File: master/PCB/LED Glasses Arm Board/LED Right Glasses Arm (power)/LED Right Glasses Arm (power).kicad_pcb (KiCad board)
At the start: 2 copper layers, 130.8 x 20.4 mm, 27 parts, among them J1 Conn_01x02_Male, J2 Conn_01x01_Male, J3 Conn_01x01_Male, Q1 TP0610T, SW1 SW_SPST, U1 TPS63061DSCT

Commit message: updated board
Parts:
- removed R5: 1M, Resistor_SMD:R_0603_1608Metric
- moved C6 7.16 mm to (178.7, 94.2), turned to 90 degrees
- moved C3 5.70 mm to (185.0, 98.4)
- moved TP_gnd1 2.44 mm to (182.5, 93.6)
- moved R3 0.92 mm to (184.2, 94.1), turned to 270 degrees
- moved R4 0.75 mm to (181.3, 97.5)
- moved R2 0.34 mm to (168.0, 98.8)
- moved D2 0.34 mm to (167.3, 95.2)
- moved C5 0.34 mm to (170.6, 95.5)
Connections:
- R2 pad 2: /PG -> GND
- TP_gnd1 pad 1: /PG -> GND
- U1 pad 5: /PG -> Net-(U1-Pad5)
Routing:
- net /VOUT_5V: track 0.00 -> 39.7 mm
- net GND: track 12.3 -> 0.09 mm, vias 8 -> 6
- net Net-(C3-Pad1): track 4.58 -> 0.00 mm
- net Net-(C5-Pad1): track 2.25 -> 0.00 mm
- net Net-(L1-Pad2): track 5.84 -> 4.32 mm
- net Net-(L1-Pad1): track 5.84 -> 4.35 mm
- net (no net): vias 0 -> 2
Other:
- net class Default: trace_width 0.25 -> 0.8; via_drill 0.4 -> 0.3

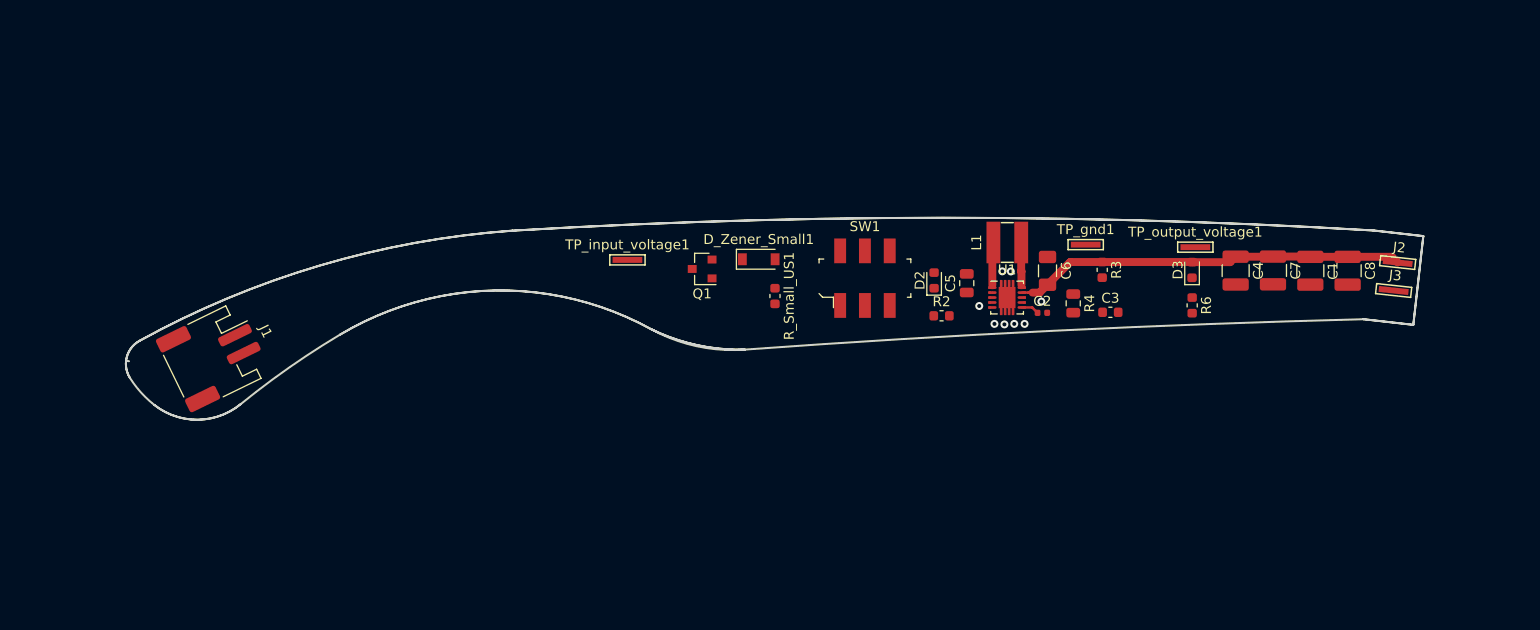
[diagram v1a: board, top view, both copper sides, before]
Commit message: Changes
Test points, routing, need to get the ground plane on the back copper
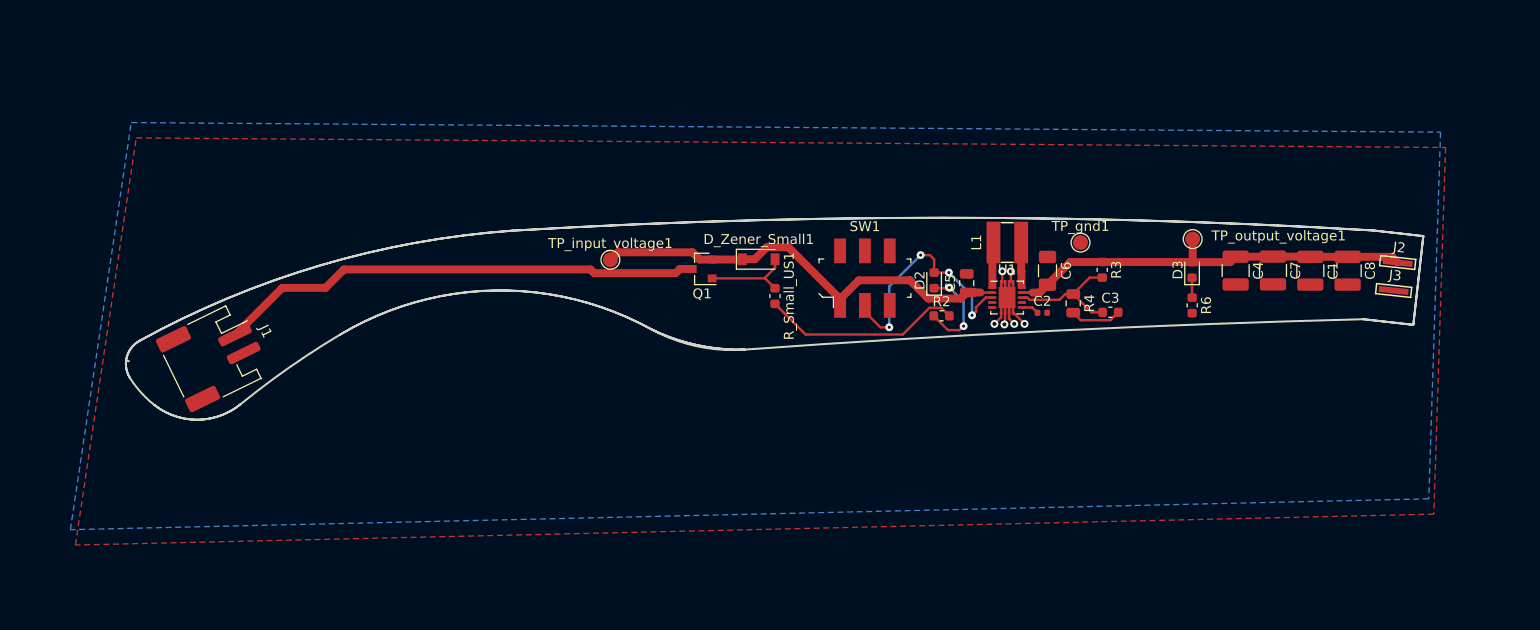
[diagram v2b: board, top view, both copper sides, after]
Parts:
- TP_gnd1, TP_input_voltage1, TP_output_voltage1: footprint Connector_PinHeader_1.00mm:PinHeader_1x01_P1.00mm_Vertical_SMD_CUSTOM -> TestPoint:TestPoint_Pad_D1.5mm
- moved TP_output_voltage1 2.86 mm to (193.3, 91.0)
- moved TP_input_voltage1 2.67 mm to (134.6, 93.1)
- moved TP_gnd1 2.30 mm to (182.0, 91.4)
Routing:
- net /VIN_2.5-12V: track 0.00 -> 49.2 mm
- net Net-(C5-Pad1): track 0.00 -> 44.2 mm
- net GND: track 0.09 -> 34.0 mm
- net Net-(D2-Pad2): track 0.00 -> 25.0 mm, vias 0 -> 4
- net Net-(C3-Pad1): track 0.00 -> 12.9 mm
- net Net-(D2-Pad1): track 0.00 -> 9.82 mm, vias 0 -> 2
- net Net-(D_Zener_Small1-Pad2): track 0.00 -> 9.10 mm
- net /VOUT_5V: track 39.7 -> 42.0 mm
- net Net-(D3-Pad1): track 0.00 -> 2.00 mm
- net (no net): vias 2 -> 0
- added copper zone on B.Cu, net GND
- added copper zone on F.Cu, net GND
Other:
- net class Default: trace_width 0.8 -> 0.25

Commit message: PCB Ready?
Thoughts and Prayers
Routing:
- net GND: track 34.0 -> 44.7 mm, vias 6 -> 10
- net Net-(D2-Pad2): track 25.0 -> 22.8 mm
- net Net-(D2-Pad1): track 9.82 -> 9.22 mm
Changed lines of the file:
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@@
     (thickness 1.6)
     (drawings 25)
-    (tracks 132)
+    (tracks 158)
     (zones 0)
     (modules 26)
@@
   (segment (start 154.318701 100.635901) (end 164.108805 100.635901) (width 0.25) (layer F.Cu) (net 2))
   (segment (start 151.2316 97.5488) (end 154.318701 100.635901) (width 0.25) (layer F.Cu) (net 2))
+  (via (at 178.689 91.186) (size 0.8) (drill 0.3) (layers F.Cu B.Cu) (net 2))
+  (segment (start 178.7017 91.1987) (end 178.689 91.186) (width 0.25) (layer F.Cu) (net 2))
+  (segment (start 174.025 97.7387) (end 174.025 98.3387) (width 0.25) (layer F.Cu) (net 2))
+  (segment (start 174.025 97.6137) (end 174.025 97.7387) (width 0.25) (layer F.Cu) (net 2))
+  (segment (start 173.825 97.4137) (end 174.025 97.6137) (width 0.25) (layer F.Cu) (net 2))
+  (segment (start 173.15 97.4137) (end 173.825 97.4137) (width 0.25) (layer F.Cu) (net 2))
+  (segment (start 175.225 97.7387) (end 175.225 98.3387) (width 0.25) (layer F.Cu) (net 2))
+  (segment (start 175.225 97.6137) (end 175.225 97.7387) (width 0.25) (layer F.Cu) (net 2))
+  (segment (start 175.425 97.4137) (end 175.225 97.6137) (width 0.25) (layer F.Cu) (net 2))
+  (segment (start 176.1 97.4137) (end 175.425 97.4137) (width 0.25) (layer F.Cu) (net 2))
+  (segment (start 174.2598 95.4887) (end 174.1424 95.3713) (width 0.25) (layer F.Cu) (net 2))
+  (segment (start 174.425 95.4887) (end 174.2598 95.4887) (width 0.25) (layer F.Cu) (net 2))
+  (segment (start 174.825 95.4507) (end 175.006 95.2697) (width 0.25) (layer F.Cu) (net 2))
+  (segment (start 174.825 95.4887) (end 174.825 95.4507) (width 0.25) (layer F.Cu) (net 2))
+  (segment (start 173.15 97.4137) (end 172.865 97.4137) (width 0.25) (layer F.Cu) (net 2))
+  (segment (start 172.61141 97.4137) (end 173.15 97.4137) (width 0.25) (layer F.Cu) (net 2))
+  (segment (start 172.39999 97.62512) (end 172.61141 97.4137) (width 0.25) (layer F.Cu) (net 2))
+  (segment (start 172.39999 97.874912) (end 172.39999 97.62512) (width 0.25) (layer F.Cu) (net 2))
+  (segment (start 171.519702 98.7552) (end 172.39999 97.874912) (width 0.25) (layer F.Cu) (net 2))
+  (segment (start 168.8085 98.7552) (end 171.519702 98.7552) (width 0.25) (layer F.Cu) (net 2))
+  (via (at 101.7524 100.7491) (size 0.8) (drill 0.3) (layers F.Cu B.Cu) (net 2))
+  (via (at 170.561 93.1672) (size 0.8) (drill 0.3) (layers F.Cu B.Cu) (net 2))
+  (segment (start 170.561 94.5284) (end 170.561 93.1672) (width 0.25) (layer F.Cu) (net 2))
+  (via (at 184.3151 91.3765) (size 0.8) (drill 0.3) (layers F.Cu B.Cu) (net 2))
   (via (at 168.8084 95.9104) (size 0.8) (drill 0.3) (layers F.Cu B.Cu) (net 3))
   (segment (start 167.2717 95.974) (end 168.7448 95.974) (width 0.25) (layer F.Cu) (net 3))
   (segment (start 168.7448 95.974) (end 168.8084 95.9104) (width 0.25) (layer F.Cu) (net 3))
-  (via (at 170.2435 99.7966) (size 0.8) (drill 0.3) (layers F.Cu B.Cu) (net 3))
   (segment (start 168.8084 95.9104) (end 170.2435 97.3455) (width 0.25) (layer B.Cu) (net 3))
-  (segment (start 170.2435 97.3455) (end 170.2435 99.7966) (width 0.25) (layer B.Cu) (net 3))
+  (via (at 169.9895 99.4802) (size 0.8) (drill 0.3) (layers F.Cu B.Cu) (net 3))
+  (segment (start 170.2435 97.3455) (end 170.2435 99.2262) (width 0.25) (layer B.Cu) (net 3))
+  (segment (start 170.2435 99.2262) (end 169.9895 99.4802) (width 0.25) (layer B.Cu) (net 3))
   (segment (start 167.695112 99.216812) (end 167.2335 98.7552) (width 0.25) (layer F.Cu) (net 3))
-  (segment (start 168.674899 100.196599) (end 167.695112 99.216812) (width 0.25) (layer F.Cu) (net 3))
-  (segment (start 169.843501 100.196599) (end 168.674899 100.196599) (width 0.25) (layer F.Cu) (net 3))
-  (segment (start 170.2435 99.7966) (end 169.843501 100.196599) (width 0.25) (layer F.Cu) (net 3))
+  (segment (start 168.358499 99.880199) (end 167.695112 99.216812) (width 0.25) (layer F.Cu) (net 3))
+  (segment (start 169.589501 99.880199) (end 168.358499 99.880199) (width 0.25) (layer F.Cu) (net 3))
+  (segment (start 169.9895 99.4802) (end 169.589501 99.880199) (width 0.25) (layer F.Cu) (net 3))
   (segment (start 193.2686 96.9009) (end 193.2813 96.9136) (width 0.25) (layer F.Cu) (net 4))
   (segment (start 193.2686 94.9199) (end 193.2686 96.9009) (width 0.25) (layer F.Cu) (net 4))
@@
   (segment (start 167.2717 94.399) (end 168.7575 94.399) (width 0.25) (layer F.Cu) (net 6))
   (segment (start 168.7575 94.399) (end 168.7576 94.3991) (width 0.25) (layer F.Cu) (net 6))
-  (via (at 171.0944 98.7044) (size 0.8) (drill 0.3) (layers F.Cu B.Cu) (net 6))
-  (segment (start 171.093299 98.703299) (end 171.0944 98.7044) (width 0.25) (layer B.Cu) (net 6))
   (segment (start 168.7576 94.3991) (end 171.093299 96.734799) (width 0.25) (layer B.Cu) (net 6))
-  (segment (start 171.093299 96.734799) (end 171.093299 98.703299) (width 0.25) (layer B.Cu) (net 6))
   (segment (start 172.475 96.9137) (end 173.15 96.9137) (width 0.25) (layer F.Cu) (net 6))
-  (segment (start 171.494399 97.894301) (end 172.475 96.9137) (width 0.25) (layer F.Cu) (net 6))
-  (segment (start 171.494399 98.304401) (end 171.494399 97.894301) (width 0.25) (layer F.Cu) (net 6))
-  (segment (start 171.0944 98.7044) (end 171.494399 98.304401) (width 0.25) (layer F.Cu) (net 6))
+  (via (at 171.6659 97.536) (size 0.8) (drill 0.3) (layers F.Cu B.Cu) (net 6))
+  (segment (start 172.07349 97.12841) (end 171.6659 97.536) (width 0.25) (layer F.Cu) (net 6))
+  (segment (start 172.475 96.9137) (end 172.26029 97.12841) (width 0.25) (layer F.Cu) (net 6))
+  (segment (start 172.26029 97.12841) (end 172.07349 97.12841) (width 0.25) (layer F.Cu) (net 6))
+  (segment (start 171.265901 96.907401) (end 171.093299 96.734799) (width 0.25) (layer B.Cu) (net 6))
+  (segment (start 171.265901 97.136001) (end 171.265901 96.907401) (width 0.25) (layer B.Cu) (net 6))
+  (segment (start 171.6659 97.536) (end 171.265901 97.136001) (width 0.25) (layer B.Cu) (net 6))
   (segment (start 177.1593 97.9137) (end 177.696 98.4504) (width 0.25) (layer F.Cu) (net 7))
   (segment (start 176.1 97.9137) (end 177.1593 97.9137) (width 0.25) (layer F.Cu) (net 7))
@@
     (polygon
       (pts
-        (xy 86.348793 79.27639) (xy 218.314493 80.24159) (xy 217.133393 117.19859) (xy 80.214693 120.31009)
+        (xy 82.7405 72.2757) (xy 75.9206 128.397) (xy 225.0821 127.1397) (xy 226.3394 70.7517)
       )
     )
@@
     (polygon
       (pts
-        (xy 86.8553 80.8228) (xy 218.821 81.788) (xy 217.6399 118.745) (xy 80.7212 121.8565)
+        (xy 82.0928 71.4375) (xy 75.1205 127.5588) (xy 223.2914 126.0729) (xy 224.917 68.9229)
       )
     )

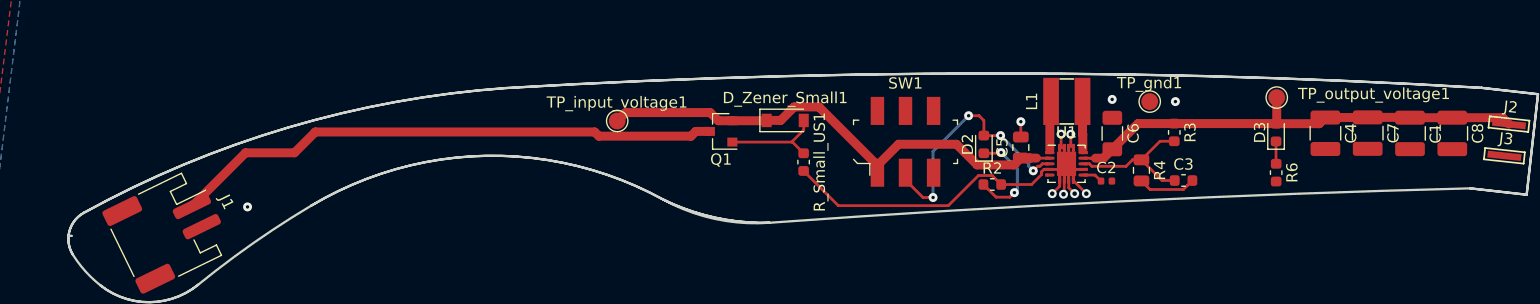
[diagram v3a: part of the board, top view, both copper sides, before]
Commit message: Made a few small cosmetic changes to labels and values (i.e. R_small_US1 to R1).
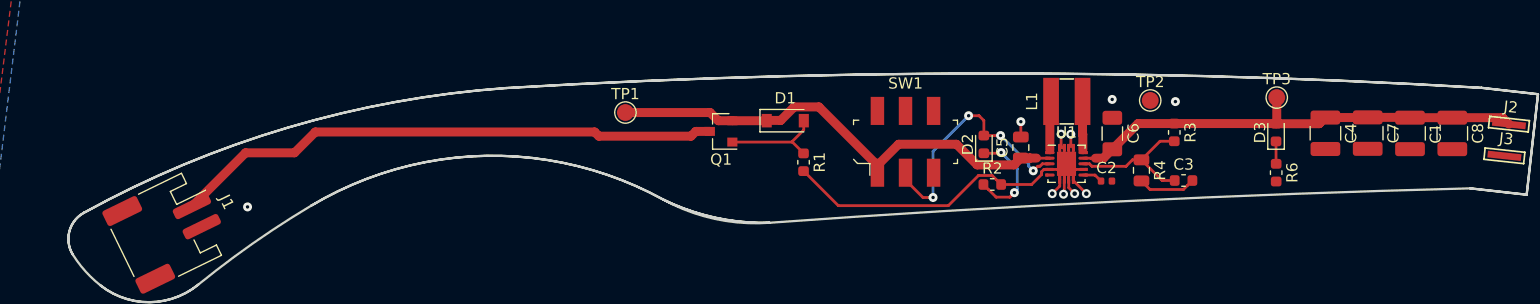
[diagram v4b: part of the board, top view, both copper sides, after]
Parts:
- removed D_Zener_Small1: 6V, Diode_SMD:D_SOD-123
- removed R_Small_US1: 100k1, Resistor_SMD:R_0603_1608Metric
- removed TP_gnd1, TP_input_voltage1, TP_output_voltage1: TestPoint, TestPoint:TestPoint_Pad_D1.5mm
- added D1: 6V, Diode_SMD:D_SOD-123, F.Cu at (149.6, 93.1)
- added R1: 100k1, Resistor_SMD:R_0603_1608Metric, F.Cu at (151.2, 96.8)
- added TP1: VIN, TestPoint:TestPoint_Pad_D1.5mm, F.Cu at (135.4, 92.3)
- added TP2: GND, TestPoint:TestPoint_Pad_D1.5mm, F.Cu at (182.1, 91.3)
- added TP3: VOUT, TestPoint:TestPoint_Pad_D1.5mm, F.Cu at (193.3, 91.0)
- C1, C4, C7, C8: value 220uF -> 220u
- C3: value 10pF -> 10p
- C5: value 22uF -> 22u
- C6: value 68uF -> 68u
- D2: value LED Red -> P_IN
- D3: value LED Green -> P_OUT
- J1: value Conn_01x02_Male -> PWR IN
- J2: value Conn_01x01_Male -> PWR OUT +
- J3: value Conn_01x01_Male -> PWR OUT -
- L1: value 1uF -> 1u
- SW1: value SW_SPST -> EN
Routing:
- net Net-(C5-Pad1): track 44.2 -> 43.2 mm
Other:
- outline, holes or cut-outs redrawn
